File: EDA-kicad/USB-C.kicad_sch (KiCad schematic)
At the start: 3 parts, among them J1 USBC-4-0-CX90MW9-24P1

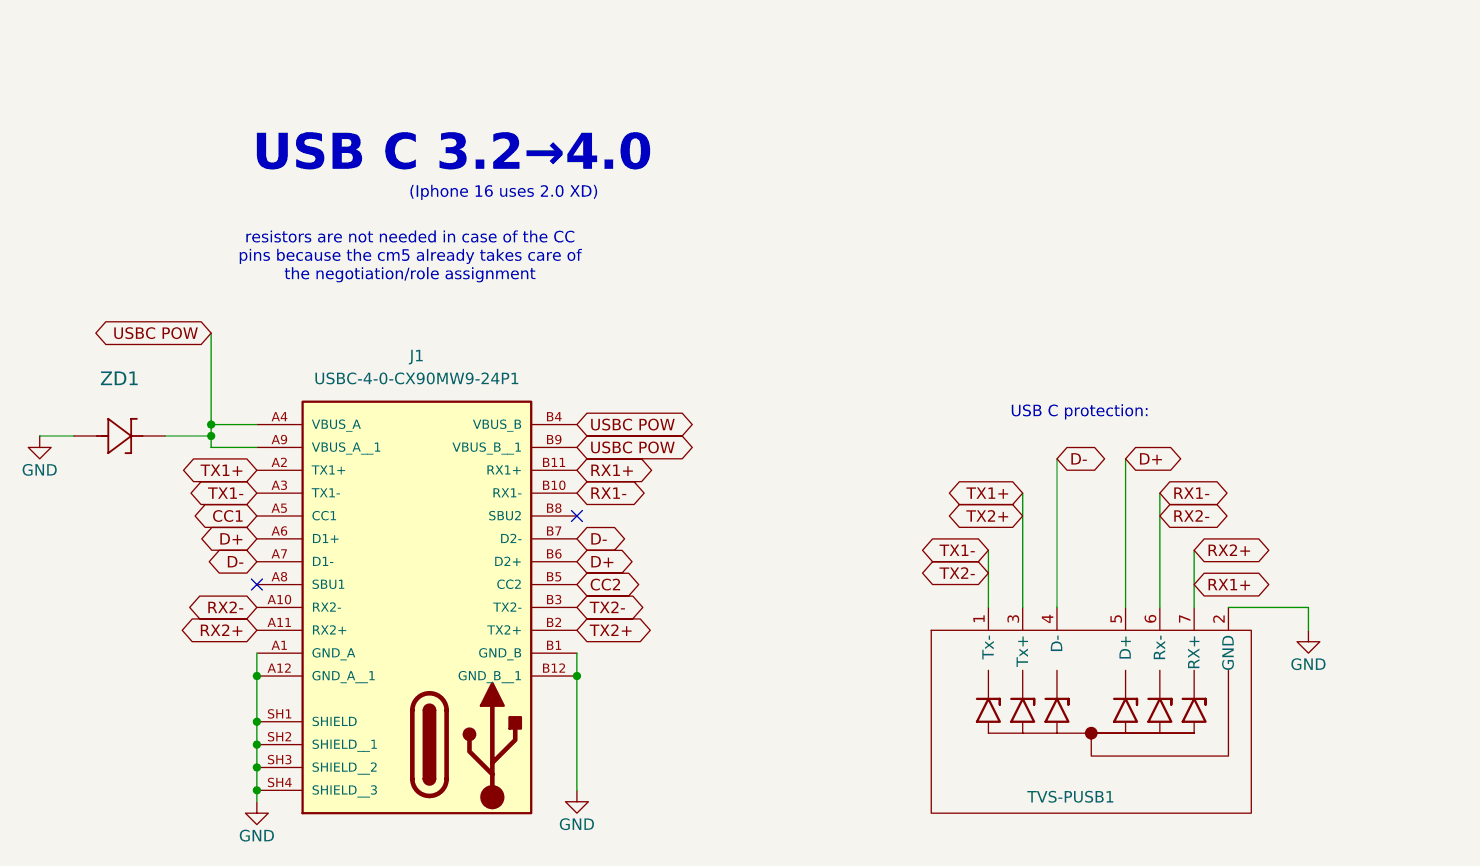
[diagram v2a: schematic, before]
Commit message: set everything except from power to DNP
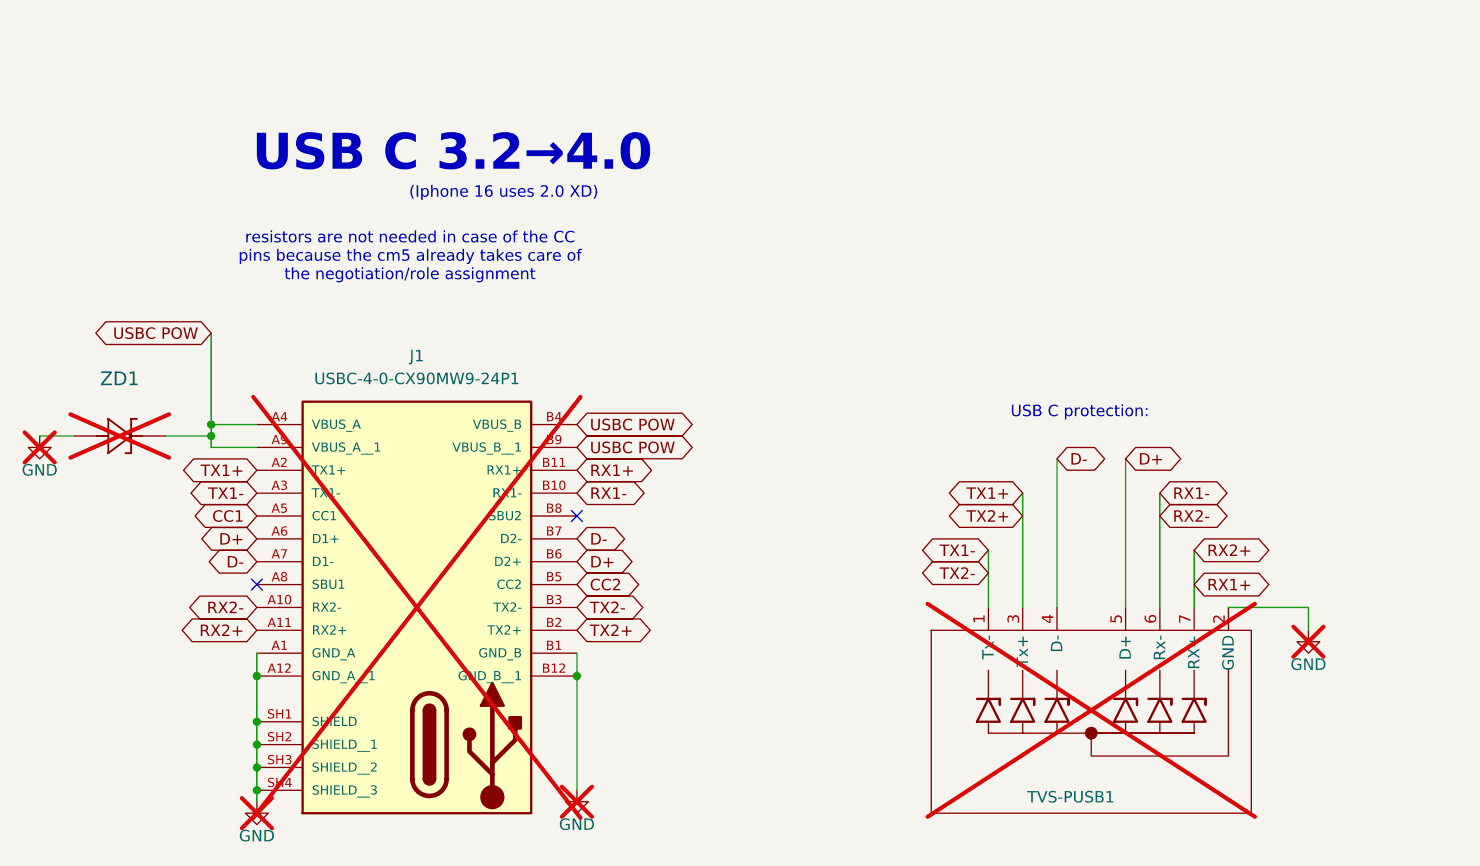
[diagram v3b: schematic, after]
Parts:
- J1, TVS-PUSB1, ZD1: now not fitted

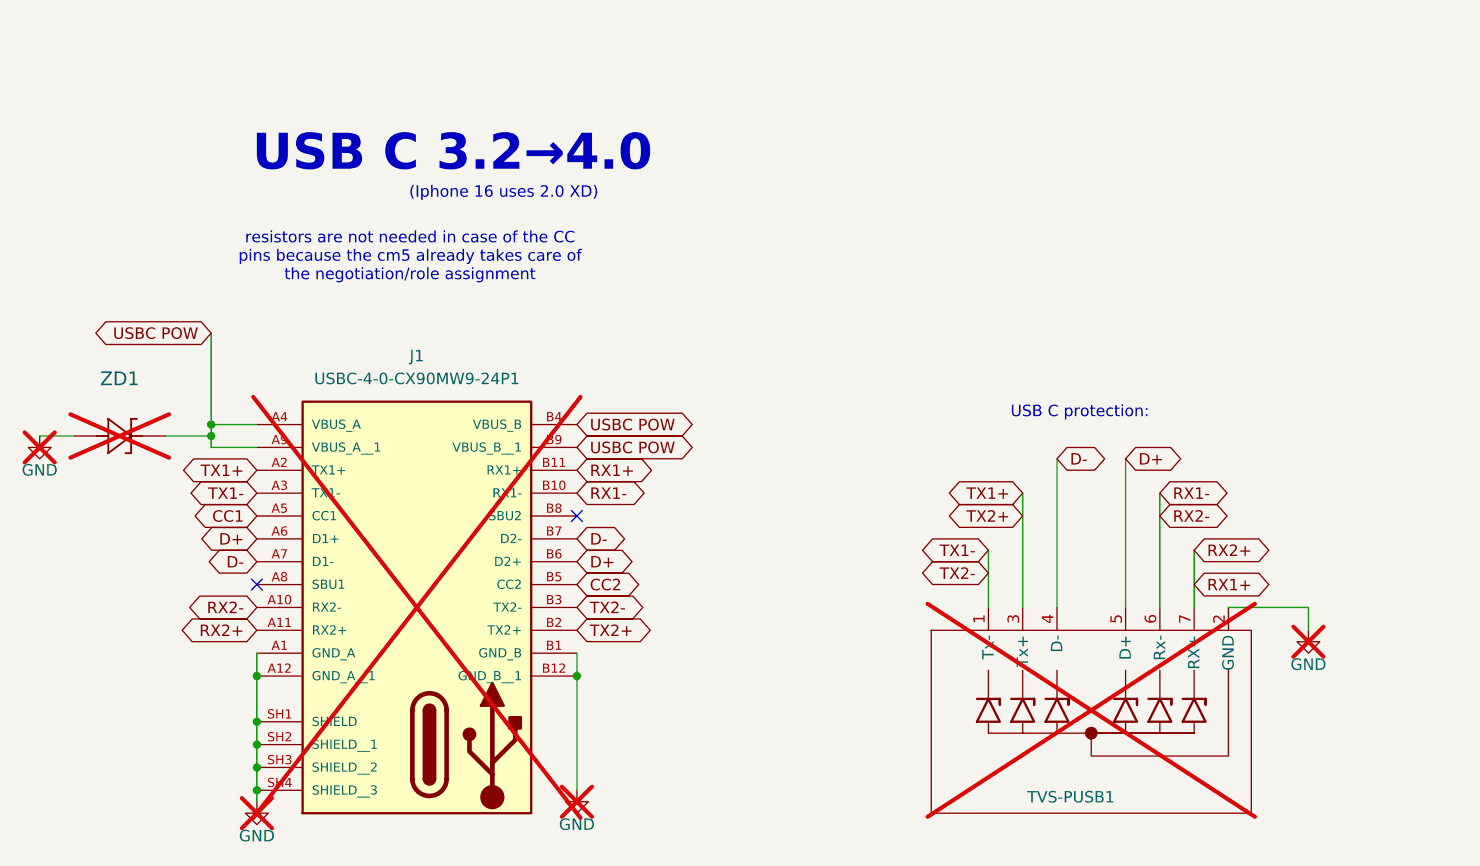
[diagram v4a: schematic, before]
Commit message: Improve KiCAD schematic design and labeling
- Replace overused global labels with hierarchical and local labels
- Add proper GND connections to components
- Fix BACKLIGHT- net issues
- Apply minor schematic fixes and cleanups
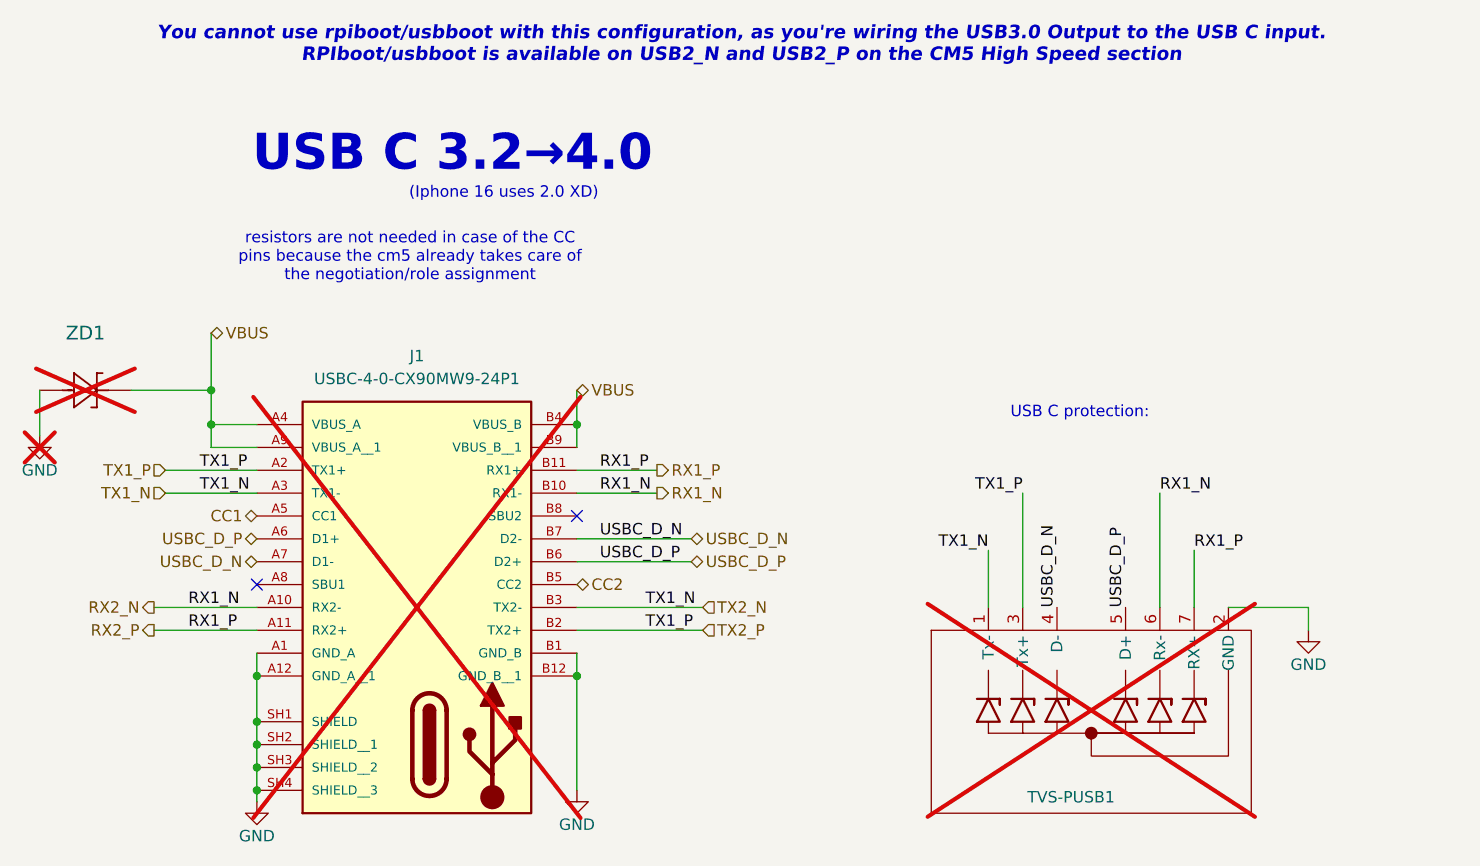
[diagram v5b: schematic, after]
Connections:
- net D+ renamed USBC_D_P
- net D- renamed USBC_D_N
- net RX1+ renamed RX1_P
- net RX1- renamed RX1_N
- net TX1+ renamed TX1_P
- net TX1- renamed TX1_N
- net USBC POW renamed VBUS
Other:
- note added: "You cannot use rpiboot/usbboot with this configuration, as you're wiring the USB3.0 Output to the USB C input. RPIboot/usbboot is available on USB2_N and USB2_P on the CM5 High Speed section"
- moved on the sheet: ZD1
